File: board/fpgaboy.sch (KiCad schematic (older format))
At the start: 83 parts, among them J1 Conn_01x12, J2 Conn_01x06, J3 Micro_SD_Card_Det, J4 Conn_01x06, P1 ILI9341, P2 CONN_01X02, P3 USB_OTG, Q1 BSS816NW, SW1 SWITCH_SPST, U1 iCE40-HX8k-BG121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

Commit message: .
Former-commit-id: 099437aeaa0f87b81eeb045cc0cc2065e57b2218 [formerly 5b995d2ac2d80979005ea056349abce62d091246]
Former-commit-id: e3da0e3630d2230d9d68ed8e3ef45ab7c693987d
Former-commit-id: aab129dfe919954ae2f0a219e0799318124eaf7d
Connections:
- net FPGA_UART_RX: now also RN1.4 (R4.1); no longer RN1.2 (R2.1)
- net FPGA_UART_TX: now also RN1.3 (R3.1); no longer RN1.1 (R1.1)
- net uSD_CLK: now also RN2.1 (R1.1); no longer RN2.2 (R2.1)
- net uSD_CMD: now also RN2.2 (R2.1); no longer RN2.1 (R1.1)
- net uSD_DAT0: now also RN1.2 (R2.1); no longer RN2.3 (R3.1)
- net uSD_DAT1: now also RN1.1 (R1.1); no longer RN2.4 (R4.1)
- net uSD_DAT2: now also RN2.3 (R3.1); no longer RN1.3 (R3.1)
- net uSD_DAT3: now also RN2.4 (R4.1); no longer RN1.4 (R4.1)
- no-connect marks 52 -> 53
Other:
- moved on the sheet: TP10, TP5, TP6, TP7, TP8, TP9
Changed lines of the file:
@@
 	1    0    0    -1
 $EndComp
-Text Label 8250 10400 2    50   ~ 0
+Text Label 8050 10400 2    50   ~ 0
 uSD_DAT0
-Text Label 8250 10500 2    50   ~ 0
+Text Label 8050 10500 2    50   ~ 0
 uSD_DAT1
-Text Label 8250 9900 2    50   ~ 0
+Text Label 8050 9900 2    50   ~ 0
 uSD_DAT3
-Text Label 8250 10000 2    50   ~ 0
+Text Label 8050 10000 2    50   ~ 0
 uSD_CMD
-Text Label 8250 10200 2    50   ~ 0
+Text Label 8050 10200 2    50   ~ 0
 uSD_CLK
 Wire Wire Line
@@
 L Connector:TestPoint TP5
 U 1 1 5C75ABC1
-P 7850 9800
-F 0 "TP5" V 7804 9988 50  0000 L CNN
-F 1 "TestPoint" V 7850 10150 50  0000 L CNN
-F 2 "fpgaboy_parts:Testpoint_d0.7mm" H 8050 9800 50  0001 C CNN
-F 3 "~" H 8050 9800 50  0001 C CNN
-	1    7850 9800
+P 7650 9800
+F 0 "TP5" V 7604 9988 50  0000 L CNN
+F 1 "TestPoint" V 7650 10150 50  0000 L CNN
+F 2 "fpgaboy_parts:Testpoint_d0.7mm" H 7850 9800 50  0001 C CNN
+F 3 "~" H 7850 9800 50  0001 C CNN
+	1    7650 9800
 	0    -1   1    0
 $EndComp
@@
 L Connector:TestPoint TP6
 U 1 1 5C75AF0D
-P 7850 9900
-F 0 "TP6" V 7804 10088 50  0000 L CNN
-F 1 "TestPoint" V 7850 10250 50  0000 L CNN
-F 2 "fpgaboy_parts:Testpoint_d0.7mm" H 8050 9900 50  0001 C CNN
-F 3 "~" H 8050 9900 50  0001 C CNN
-	1    7850 9900
+P 7650 9900
+F 0 "TP6" V 7604 10088 50  0000 L CNN
+F 1 "TestPoint" V 7650 10250 50  0000 L CNN
+F 2 "fpgaboy_parts:Testpoint_d0.7mm" H 7850 9900 50  0001 C CNN
+F 3 "~" H 7850 9900 50  0001 C CNN
+	1    7650 9900
 	0    -1   1    0
 $EndComp
@@
 L Connector:TestPoint TP7
 U 1 1 5C75AFE4
-P 7850 10000
-F 0 "TP7" V 7804 10188 50  0000 L CNN
-F 1 "TestPoint" V 7850 10350 50  0000 L CNN
-F 2 "fpgaboy_parts:Testpoint_d0.7mm" H 8050 10000 50  0001 C CNN
-F 3 "~" H 8050 10000 50  0001 C CNN
-	1    7850 10000
+P 7650 10000
+F 0 "TP7" V 7604 10188 50  0000 L CNN
+F 1 "TestPoint" V 7650 10350 50  0000 L CNN
+F 2 "fpgaboy_parts:Testpoint_d0.7mm" H 7850 10000 50  0001 C CNN
+F 3 "~" H 7850 10000 50  0001 C CNN
+	1    7650 10000
 	0    -1   1    0
 $EndComp
@@
 L Connector:TestPoint TP8
 U 1 1 5C75B09D
-P 7850 10200
-F 0 "TP8" V 7804 10388 50  0000 L CNN
-F 1 "TestPoint" V 7850 10550 50  0000 L CNN
-F 2 "fpgaboy_parts:Testpoint_d0.7mm" H 8050 10200 50  0001 C CNN
-F 3 "~" H 8050 10200 50  0001 C CNN
-	1    7850 10200
+P 7650 10200
+F 0 "TP8" V 7604 10388 50  0000 L CNN
+F 1 "TestPoint" V 7650 10550 50  0000 L CNN
+F 2 "fpgaboy_parts:Testpoint_d0.7mm" H 7850 10200 50  0001 C CNN
+F 3 "~" H 7850 10200 50  0001 C CNN
+	1    7650 10200
 	0    -1   1    0
 $EndComp
@@
 L Connector:TestPoint TP9
 U 1 1 5C75B146
-P 7850 10400
-F 0 "TP9" V 7804 10588 50  0000 L CNN
-F 1 "TestPoint" V 7850 10750 50  0000 L CNN
-F 2 "fpgaboy_parts:Testpoint_d0.7mm" H 8050 10400 50  0001 C CNN
-F 3 "~" H 8050 10400 50  0001 C CNN
-	1    7850 10400
+P 7650 10400
+F 0 "TP9" V 7604 10588 50  0000 L CNN
+F 1 "TestPoint" V 7650 10750 50  0000 L CNN
+F 2 "fpgaboy_parts:Testpoint_d0.7mm" H 7850 10400 50  0001 C CNN
+F 3 "~" H 7850 10400 50  0001 C CNN
+	1    7650 10400
 	0    -1   1    0
 $EndComp
@@
 L Connector:TestPoint TP10
 U 1 1 5C75B1F1
-P 7850 10500
-F 0 "TP10" V 7804 10688 50  0000 L CNN
-F 1 "TestPoint" V 7850 10850 50  0000 L CNN
-F 2 "fpgaboy_parts:Testpoint_d0.7mm" H 8050 10500 50  0001 C CNN
-F 3 "~" H 8050 10500 50  0001 C CNN
-	1    7850 10500
+P 7650 10500
+F 0 "TP10" V 7604 10688 50  0000 L CNN
+F 1 "TestPoint" V 7650 10850 50  0000 L CNN
+F 2 "fpgaboy_parts:Testpoint_d0.7mm" H 7850 10500 50  0001 C CNN
+F 3 "~" H 7850 10500 50  0001 C CNN
+	1    7650 10500
 	0    -1   1    0
 $EndComp
@@
 NoConn ~ 14500 9300
 NoConn ~ 14500 9400
-Text Label 8250 9800 2    50   ~ 0
+Text Label 8050 9800 2    50   ~ 0
 uSD_DAT2
 Wire Wire Line
 	9350 9100 9350 10100
-Wire Wire Line
-	9050 10500 9450 10500
-Wire Wire Line
-	8950 10400 9450 10400
-Wire Wire Line
-	8850 10200 9450 10200
-Wire Wire Line
-	8450 9900 9450 9900
-Wire Wire Line
-	8350 9800 9450 9800
-Wire Wire Line
-	9050 9450 9050 10500
-Wire Wire Line
-	8950 9450 8950 10400
-Wire Wire Line
-	8850 9450 8850 10200
-Wire Wire Line
-	8750 9450 8750 10000
-Wire Wire Line
-	8750 10000 9450 10000
-Wire Wire Line
-	8450 9450 8450 9900
-Wire Wire Line
-	8350 9450 8350 9800
-Wire Wire Line
-	8350 9800 7850 9800
-Connection ~ 8350 9800
-Wire Wire Line
-	8450 9900 7850 9900
-Connection ~ 8450 9900
-Wire Wire Line
-	8750 10000 7850 10000
-Connection ~ 8750 10000
-Wire Wire Line
-	7850 10200 8850 10200
-Connection ~ 8850 10200
-Wire Wire Line
-	8950 10400 7850 10400
-Connection ~ 8950 10400
-Wire Wire Line
-	7850 10500 9050 10500
-Connection ~ 9050 10500
-Wire Wire Line
-	8250 9450 8250 9550
 $Comp
 L Device:R_Pack04 RN2
@@
 Wire Wire Line
 	6000 3950 6000 4550
-Text Label 7850 9450 2    50   ~ 0
+Text Label 7850 9500 2    50   ~ 0
 FPGA_UART_TX
-Text Label 7850 9550 2    50   ~ 0
+Text Label 7850 9600 2    50   ~ 0
 FPGA_UART_RX
-Wire Wire Line
-	8150 9450 7850 9450
-Wire Wire Line
-	8250 9550 7850 9550
 Wire Wire Line
 	5000 2100 5800 2100
@@
 NoConn ~ 1550 4950
 NoConn ~ 1550 5050
+NoConn ~ 3100 8000
+Wire Wire Line
+	8350 9500 8350 9450
+Wire Wire Line
+	7850 9500 8350 9500
+Wire Wire Line
+	8450 9600 8450 9450
+Wire Wire Line
+	7850 9600 8450 9600
+Wire Wire Line
+	7650 9800 8950 9800
+Wire Wire Line
+	8750 9450 8750 10200
+Wire Wire Line
+	7650 10400 8250 10400
+Wire Wire Line
+	7650 10500 8150 10500
+Wire Wire Line
+	7650 10200 8750 10200
+Wire Wire Line
+	7650 10000 8850 10000
+Wire Wire Line
+	7650 9900 9050 9900
+Connection ~ 8750 10200
+Wire Wire Line
+	8750 10200 9450 10200
+Wire Wire Line
+	8850 9450 8850 10000
+Connection ~ 8850 10000
+Wire Wire Line
+	8850 10000 9450 10000
+Wire Wire Line
+	8950 9450 8950 9800
+Connection ~ 8950 9800
+Wire Wire Line
+	8950 9800 9450 9800
+Wire Wire Line
+	9050 9450 9050 9900
+Connection ~ 9050 9900
+Wire Wire Line
+	9050 9900 9450 9900
+Wire Wire Line
+	8150 9450 8150 10500
+Connection ~ 8150 10500
+Wire Wire Line
+	8150 10500 9450 10500
+Wire Wire Line
+	8250 9450 8250 10400
+Connection ~ 8250 10400
+Wire Wire Line
+	8250 10400 9450 10400
 $EndSCHEMATC

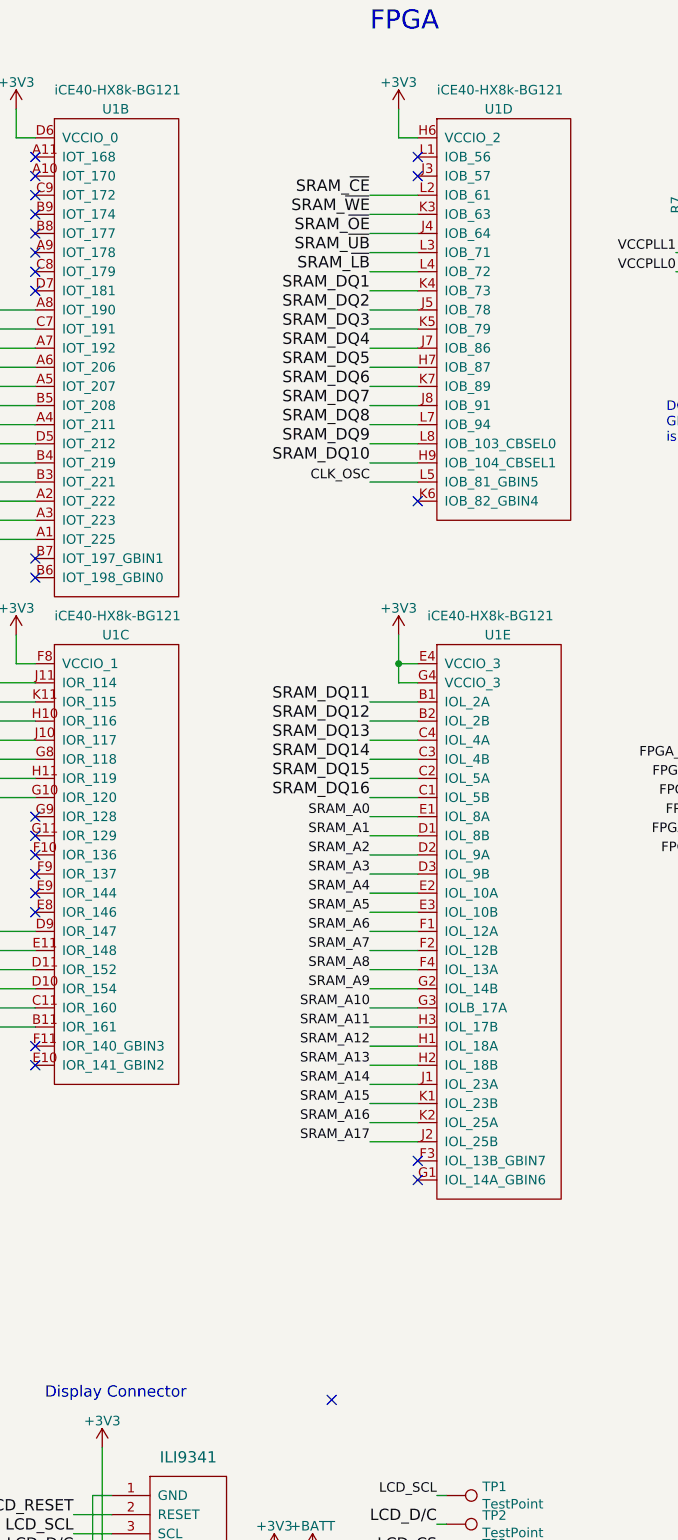
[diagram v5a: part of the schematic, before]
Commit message: BGA route out 99%. Use a gbin for an SRAM pin to avoid nasty route-out.
Former-commit-id: 07f92fcfe0b8196dbaa0211e318f2cb0094c4f09 [formerly 87ade9239a6d7c42a9d86e2b403b5dd729dbe203]
Former-commit-id: 3d668f6e0e5d229a5cfefa9fffbb2161422c9dee
Former-commit-id: 99b8390e32f2fc2be4ea2818cc2b91bb5d9c6d22
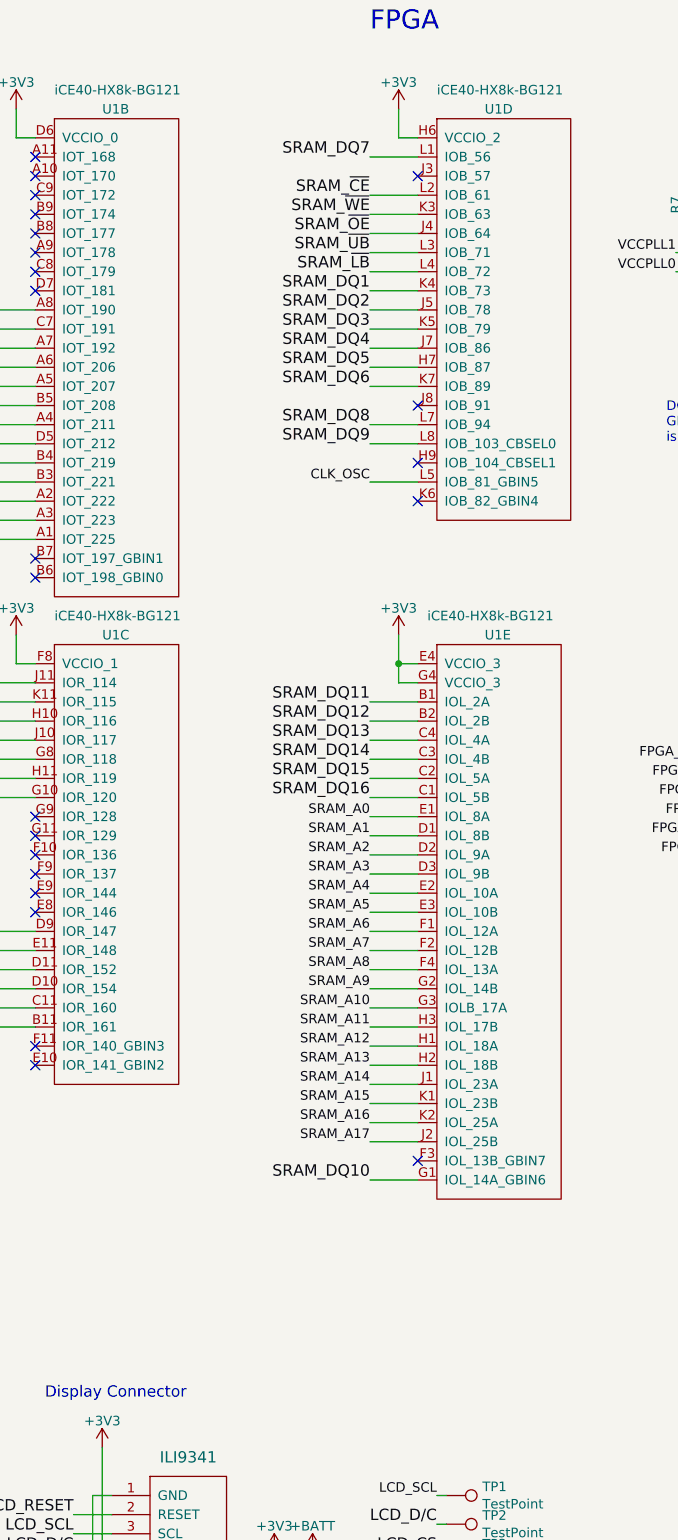
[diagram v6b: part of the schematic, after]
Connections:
- net SRAM_DQ10: now also U1.G1 (IOL_14A_GBIN6); no longer U1.H9 (IOB_104_CBSEL1)
- net SRAM_DQ7: now also U1.L1 (IOB_56); no longer U1.J8 (IOB_91)
- no-connect marks 53 -> 52
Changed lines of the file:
@@
 Text Label 3300 2700 2    60   ~ 0
 SRAM_DQ6
-Text Label 3300 2800 2    60   ~ 0
+Text Label 3300 1500 2    60   ~ 0
 SRAM_DQ7
 Text Label 3300 2900 2    60   ~ 0
@@
 Text Label 3300 3000 2    60   ~ 0
 SRAM_DQ9
-Text Label 3300 3100 2    60   ~ 0
+Text Label 3300 6850 2    60   ~ 0
 SRAM_DQ10
 Wire Wire Line
@@
 	3550 2700 3300 2700
 Wire Wire Line
-	3550 2800 3300 2800
+	3550 1500 3300 1500
 Wire Wire Line
 	3550 2900 3300 2900
@@
 	3550 3000 3300 3000
 Wire Wire Line
-	3550 3100 3300 3100
+	3550 6850 3300 6850
 Text Label 8350 4450 2    60   ~ 0
 SRAM_A0
@@
 Text Label 3300 3200 2    50   ~ 0
 CLK_OSC
-NoConn ~ 3550 1500
 NoConn ~ 3550 1600
 NoConn ~ 1550 1500
@@
 NoConn ~ 3550 3300
 NoConn ~ 3550 6750
-NoConn ~ 3550 6850
 NoConn ~ 1550 6150
 NoConn ~ 1550 6250
@@
 NoConn ~ 1550 4950
 NoConn ~ 1550 5050
-NoConn ~ 3100 8000
 Wire Wire Line
 	8350 9500 8350 9450
@@
 Wire Wire Line
 	8250 10400 9450 10400
+NoConn ~ 3550 3100
+NoConn ~ 3550 2800
 $EndSCHEMATC
